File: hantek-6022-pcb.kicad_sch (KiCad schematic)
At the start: 15 parts, among them J1 R17, J2 BNC_A, J3 BNC_B, J4 R27, J5 AC_B, J6 AC_A, J7 GND, U1 TLP175A, U2 TLP175A

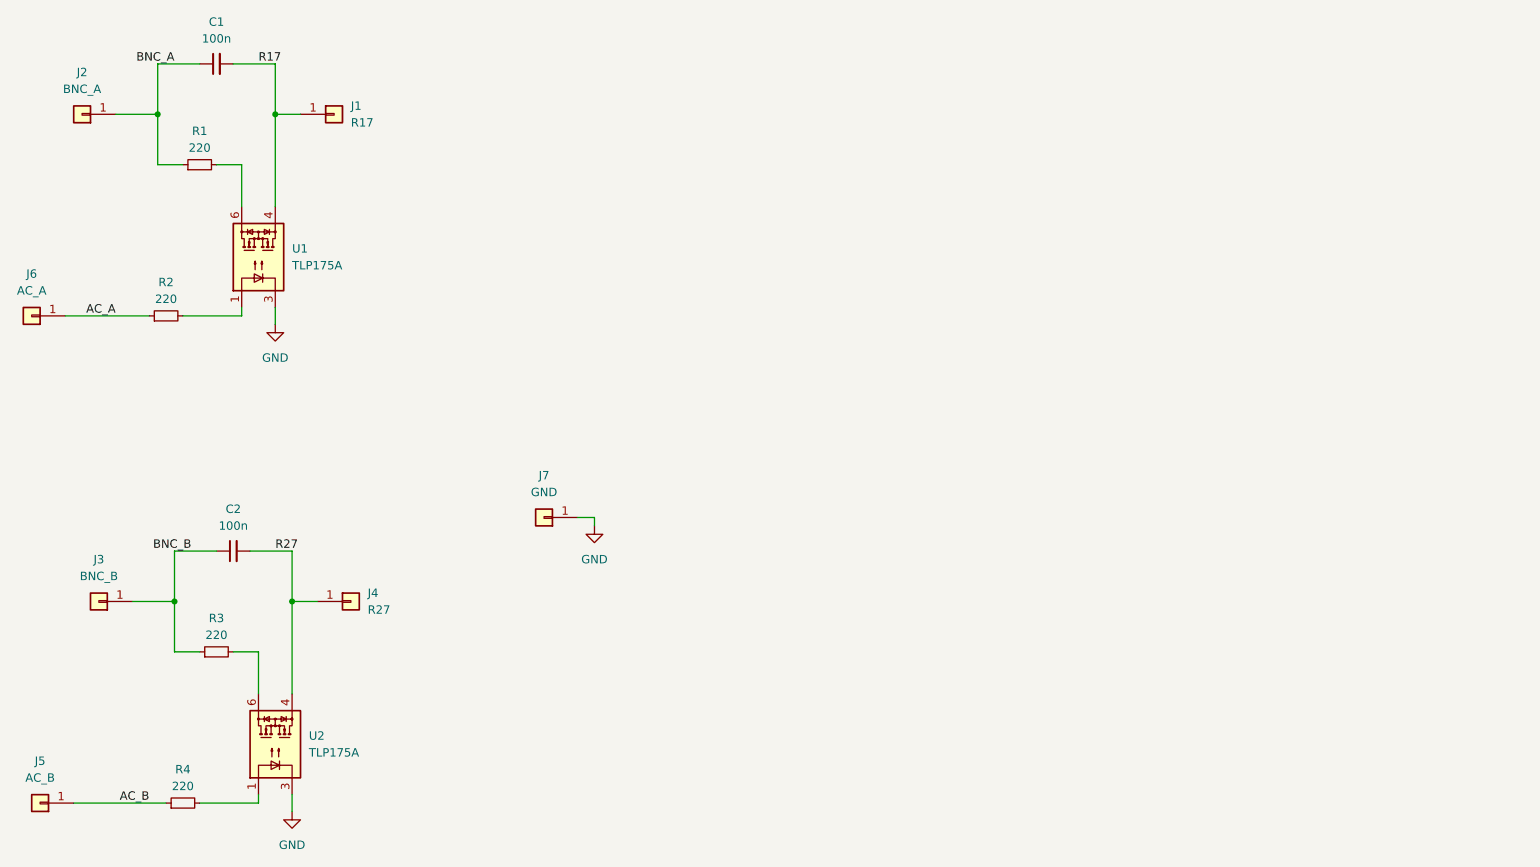
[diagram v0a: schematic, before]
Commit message: reduce pcb size, add readme
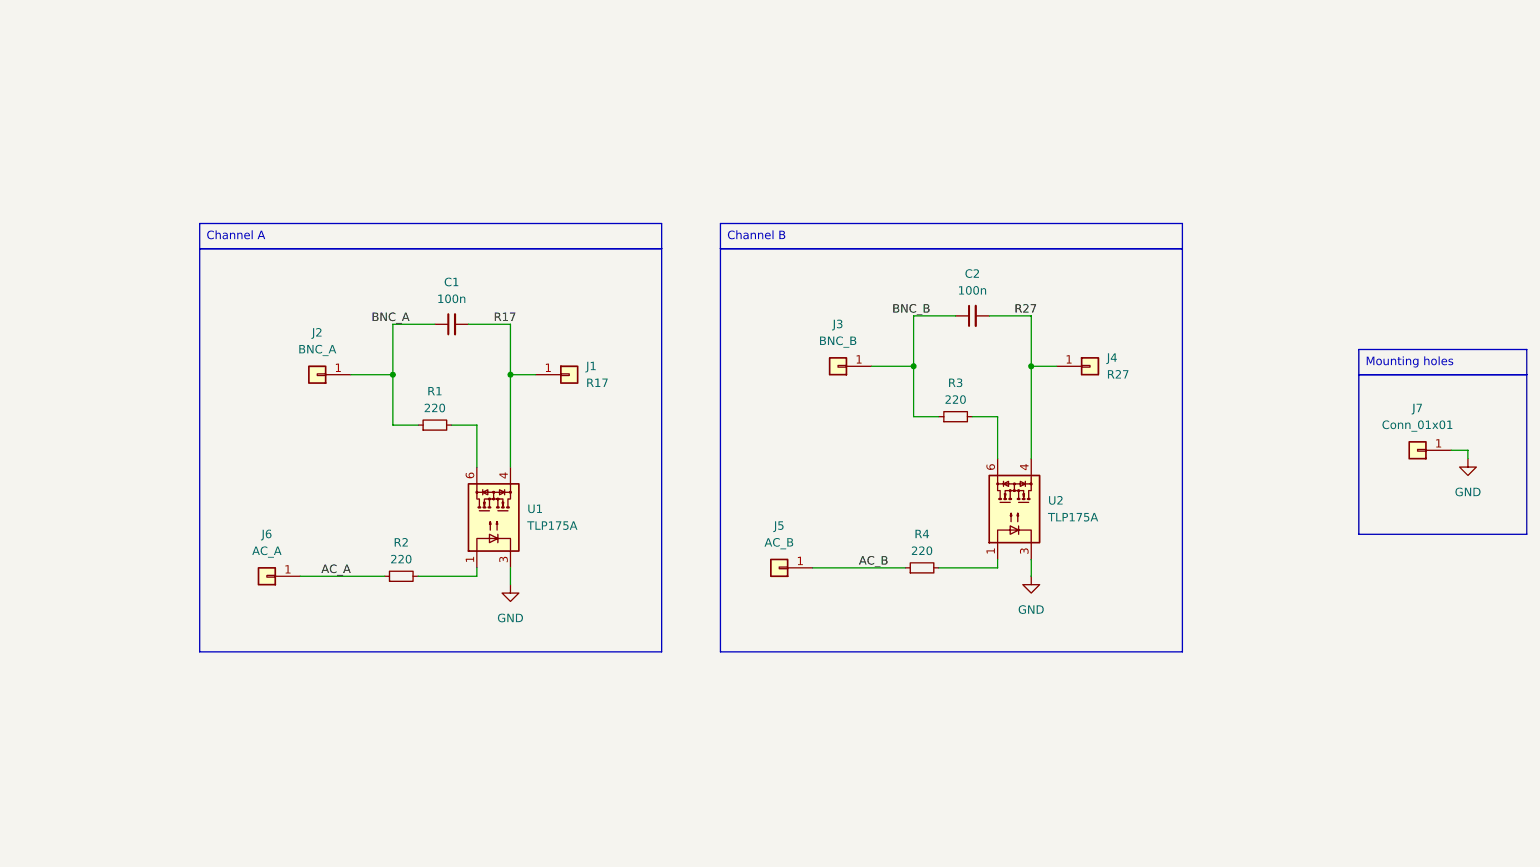
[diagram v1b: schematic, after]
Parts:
- J7: value GND -> Conn_01x01; footprint Connector_Pin:Pin_D1.0mm_L10.0mm -> Connector_PinHeader_2.54mm:PinHeader_1x01_P2.54mm_Vertical
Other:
- moved on the sheet: C1, C2, J1, J2, J3, J4, J5, J6, R1, R2, R3, R4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
